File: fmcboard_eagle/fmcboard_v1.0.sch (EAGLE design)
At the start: 50 parts, among them IC1 OPA699ID, IC2 OPA699ID, IC3 ICL7660CPA, IC4 ICL7660CPA, J1 8pin, J12 4p-2.54, J2 ASP-134604-01, J3 4p-2.54, J4 4p-2.54, J5 8pin, U1 TXS0108EPWR

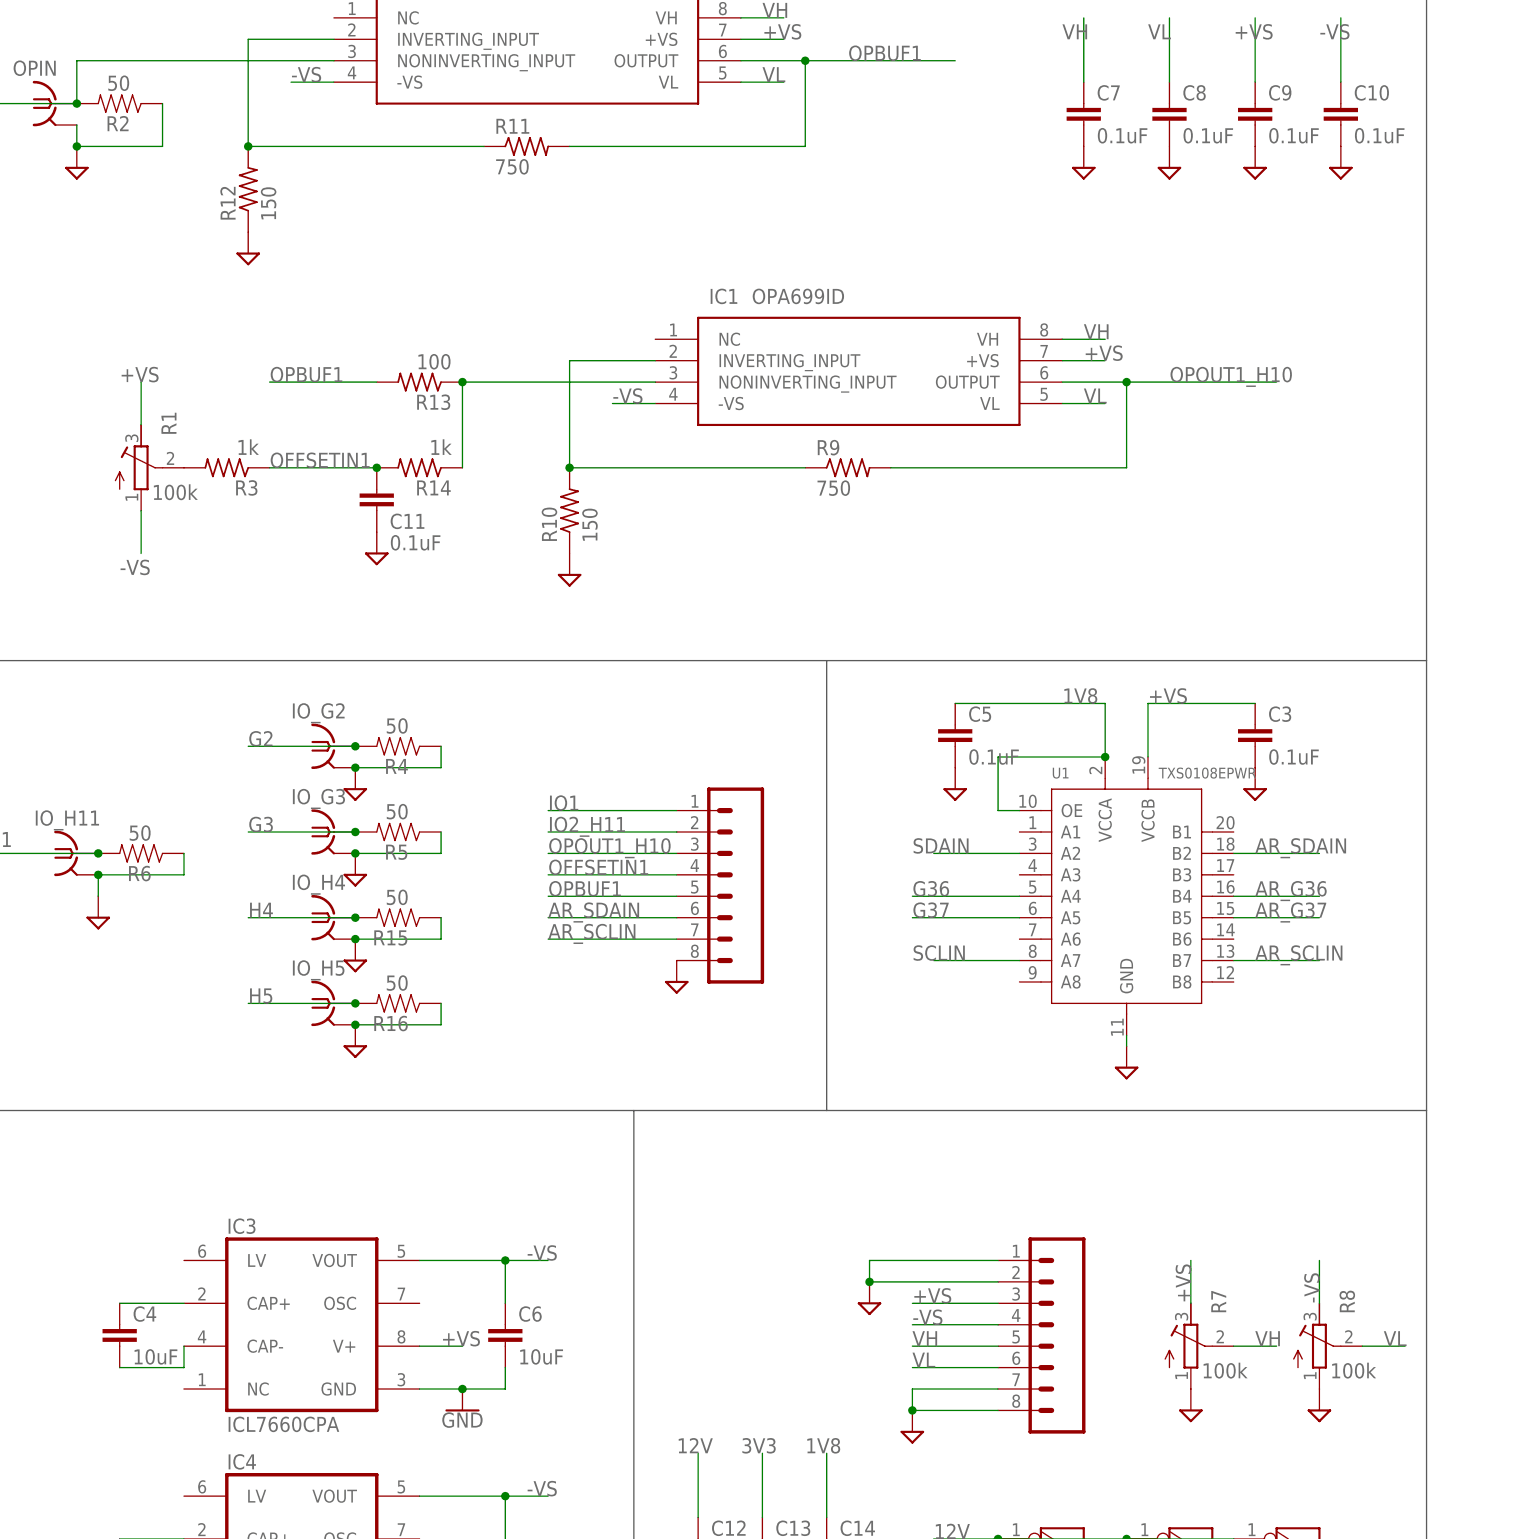
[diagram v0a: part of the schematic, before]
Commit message: Update resistor values
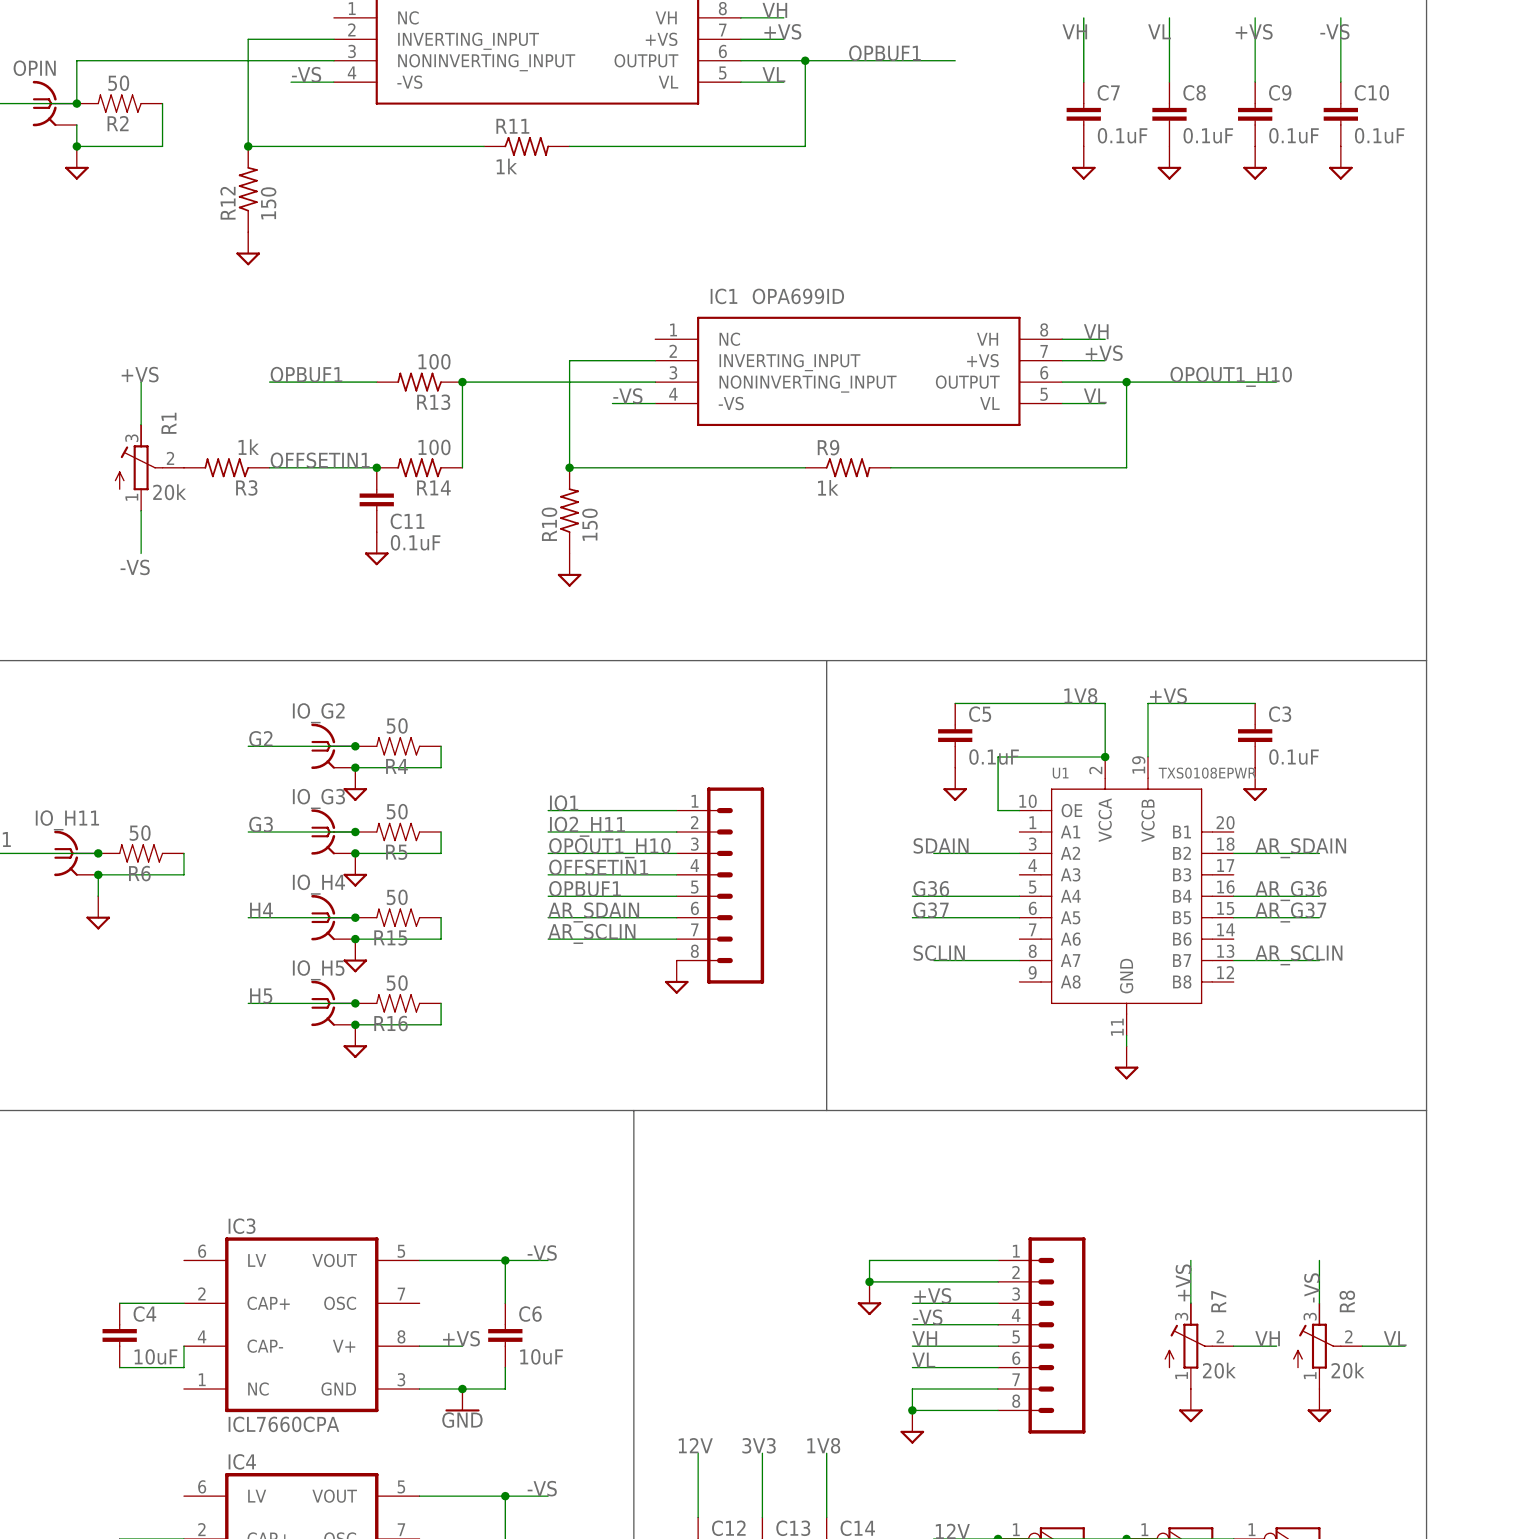
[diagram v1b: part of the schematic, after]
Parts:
- R1, R7, R8: value 100k -> 20k
- R11, R9: value 750 -> 1k
- R14: value 1k -> 100
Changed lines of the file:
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@@
 <part name="SUPPLY20" library="supply2" library_urn="urn:adsk.eagle:library:372" deviceset="GND" device=""/>
 <part name="SUPPLY21" library="supply2" library_urn="urn:adsk.eagle:library:372" deviceset="GND" device=""/>
-<part name="R7" library="resistor" library_urn="urn:adsk.eagle:library:348" deviceset="R-TRIMM" device="3296W" package3d_urn="urn:adsk.eagle:package:26033/1" value="100k"/>
-<part name="R8" library="resistor" library_urn="urn:adsk.eagle:library:348" deviceset="R-TRIMM" device="3296W" package3d_urn="urn:adsk.eagle:package:26033/1" value="100k"/>
+<part name="R7" library="resistor" library_urn="urn:adsk.eagle:library:348" deviceset="R-TRIMM" device="3296W" package3d_urn="urn:adsk.eagle:package:26033/1" value="20k"/>
+<part name="R8" library="resistor" library_urn="urn:adsk.eagle:library:348" deviceset="R-TRIMM" device="3296W" package3d_urn="urn:adsk.eagle:package:26033/1" value="20k"/>
 <part name="SUPPLY22" library="supply2" library_urn="urn:adsk.eagle:library:372" deviceset="GND" device=""/>
 <part name="SUPPLY23" library="supply2" library_urn="urn:adsk.eagle:library:372" deviceset="GND" device=""/>
 <part name="SUPPLY24" library="supply2" library_urn="urn:adsk.eagle:library:372" deviceset="GND" device=""/>
 <part name="ARDUINO_NANO1" library="ArduinoNanoV30" deviceset="ARDUINO_NANO" device=""/>
-<part name="R9" library="rcl" library_urn="urn:adsk.eagle:library:334" deviceset="R-US_" device="R0805" package3d_urn="urn:adsk.eagle:package:23553/2" value="750"/>
+<part name="R9" library="rcl" library_urn="urn:adsk.eagle:library:334" deviceset="R-US_" device="R0805" package3d_urn="urn:adsk.eagle:package:23553/2" value="1k"/>
 <part name="R10" library="rcl" library_urn="urn:adsk.eagle:library:334" deviceset="R-US_" device="R0805" package3d_urn="urn:adsk.eagle:package:23553/2" value="150"/>
-<part name="R11" library="rcl" library_urn="urn:adsk.eagle:library:334" deviceset="R-US_" device="R0805" package3d_urn="urn:adsk.eagle:package:23553/2" value="750"/>
+<part name="R11" library="rcl" library_urn="urn:adsk.eagle:library:334" deviceset="R-US_" device="R0805" package3d_urn="urn:adsk.eagle:package:23553/2" value="1k"/>
 <part name="R12" library="rcl" library_urn="urn:adsk.eagle:library:334" deviceset="R-US_" device="R0805" package3d_urn="urn:adsk.eagle:package:23553/2" value="150"/>
 <part name="R13" library="rcl" library_urn="urn:adsk.eagle:library:334" deviceset="R-US_" device="R0805" package3d_urn="urn:adsk.eagle:package:23553/2" value="100"/>
-<part name="R14" library="rcl" library_urn="urn:adsk.eagle:library:334" deviceset="R-US_" device="R0805" package3d_urn="urn:adsk.eagle:package:23553/2" value="1k"/>
+<part name="R14" library="rcl" library_urn="urn:adsk.eagle:library:334" deviceset="R-US_" device="R0805" package3d_urn="urn:adsk.eagle:package:23553/2" value="100"/>
 <part name="SUPPLY25" library="supply2" library_urn="urn:adsk.eagle:library:372" deviceset="GND" device=""/>
-<part name="R1" library="resistor" library_urn="urn:adsk.eagle:library:348" deviceset="R-TRIMM" device="3296W" package3d_urn="urn:adsk.eagle:package:26033/1" value="100k"/>
+<part name="R1" library="resistor" library_urn="urn:adsk.eagle:library:348" deviceset="R-TRIMM" device="3296W" package3d_urn="urn:adsk.eagle:package:26033/1" value="20k"/>
 <part name="R3" library="rcl" library_urn="urn:adsk.eagle:library:334" deviceset="R-US_" device="R0805" package3d_urn="urn:adsk.eagle:package:23553/2" value="1k"/>
 <part name="IO_G2" library="con-coax" library_urn="urn:adsk.eagle:library:133" deviceset="BU-SMB-V" device="" package3d_urn="urn:adsk.eagle:package:6209/1"/>

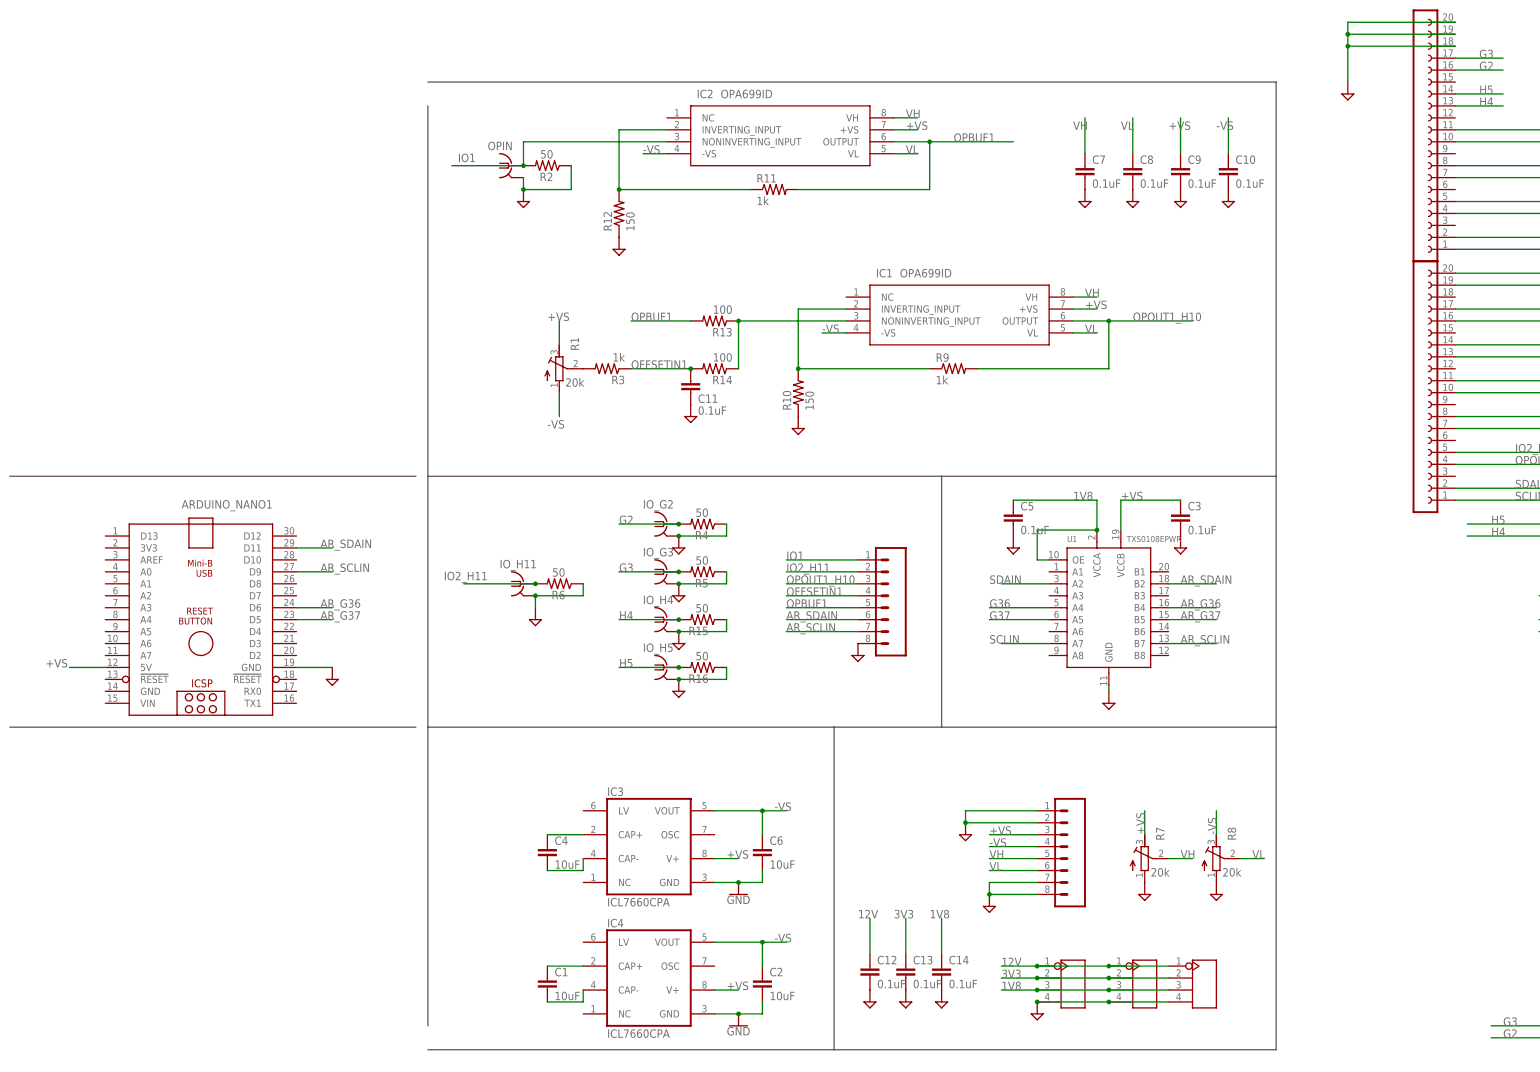
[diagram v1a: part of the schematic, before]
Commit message: add lm358 op amp buffer for offset
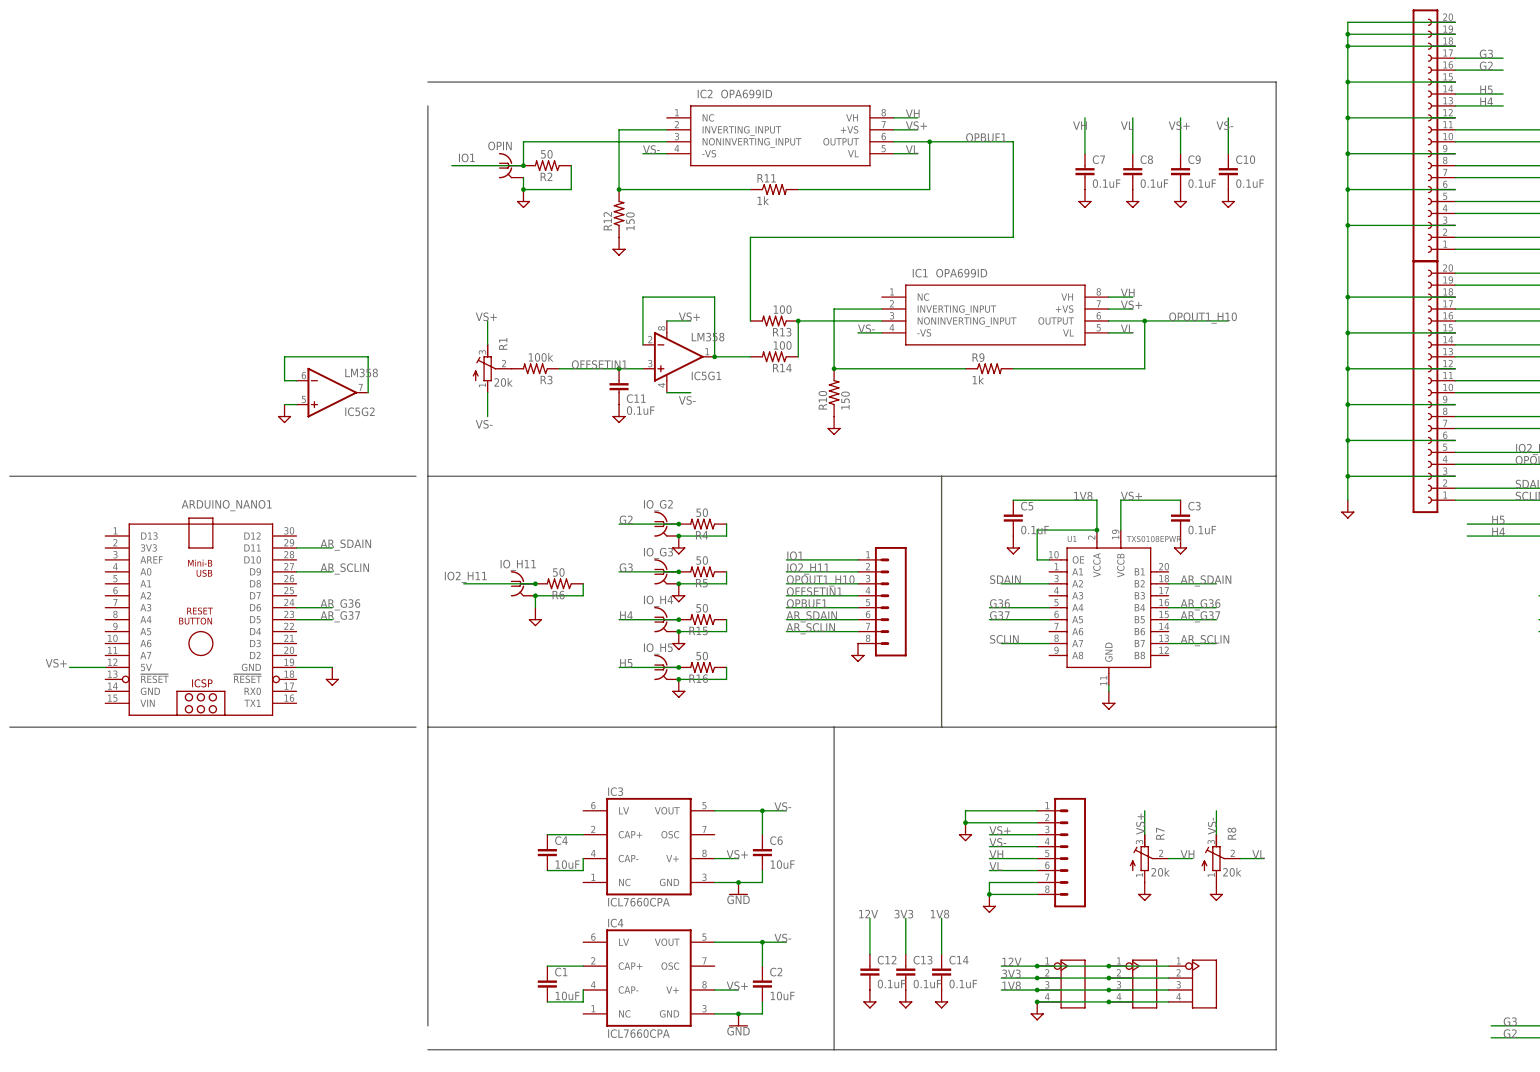
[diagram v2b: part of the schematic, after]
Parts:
- added IC5: LM358, SparkFun-AnalogIC:LM358
- R3: value 1k -> 100k
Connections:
- removed net +VS: ARDUINO_NANO1.5V, C3.1, C9.1, IC1.+VS, IC2.+VS, IC3.V+, IC4.V+, J1.3, R1.E, R7.E, U1.VCCB
- removed net -VS: C10.1, C2.1, C6.1, IC1.-VS, IC2.-VS, IC3.VOUT, IC4.VOUT, J1.4, R1.A, R8.E
- new net N$9: IC5G2.-IN, IC5G2.OUT
- new net VIN1: IC5G1.-IN, IC5G1.OUT, R14.2
- new net VS+: ARDUINO_NANO1.5V, C3.1, C9.1, IC1.+VS, IC2.+VS, IC3.V+, IC4.V+, IC5G1.V+, J1.3, R1.E, R7.E, U1.VCCB
- new net VS-: C10.1, C2.1, C6.1, IC1.-VS, IC2.-VS, IC3.VOUT, IC4.VOUT, IC5G1.V-, J1.4, R1.A, R8.E
- net GND: now also IC5G2.+IN, SV1.12, SV1.15, SV1.18, SV1.3, SV1.6, SV1.9, SV2.12, SV2.15, SV2.3, SV2.6, SV2.9
- net OFFSETIN1: now also IC5G1.+IN; no longer R14.2
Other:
- note added: "Extra op amp"
- note added: "Op amps and offset"
- note removed: "Op amps"
- moved on the sheet: C11, IC1, R1, R10, R13, R14, R3, R9
